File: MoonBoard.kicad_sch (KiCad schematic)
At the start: 52 parts, among them J1 TRRS, SW1 SW_SPST, SW2 SW_DIP_x04, U1 AMS1117-3.3, U2 74LS08, U3 STM32F303CBTx, Y1 16MHz

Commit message: tvs & less fun
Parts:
- removed J1: TRRS, Connector_Audio:Jack_3.5mm_PJ320E_Horizontal, symbol Connector_Audio:AudioJack4
- removed NT1: NetTie_2, NetTie:NetTie-2_SMD_Pad0.5mm, symbol Device:NetTie_2
- removed R1, R2, R3, R6, R7: 22, Resistor_SMD:R_0603_1608Metric, symbol Device:R_Small
- added U5 (x3): H5VU25U, MoonBoard:DFN2510, symbol Unified-Daughterboard-rescue:TPD4E05U06DQAR-acheronSymbols
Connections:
- net BOOT0: now also JP2.2 (B)
- net ENCODER_A: now also U5.1 (IO1), U5.10 (NC)
- net ENCODER_B: now also U5.2 (IO2), U5.9 (NC)
- net ENCODER_SW: now also ENCODER1.S2, U3.4 (PC15), U5.5 (D2-), U5.6 (NC); no longer ENCODER1.S1, U3.18 (PB0)
- net GND: now also ENCODER1.S1, U5.3 (GND), U5.3 (GND), U5.3 (GND), U5.8 (GND), U5.8 (GND), U5.8 (GND); no longer ENCODER1.S2
- net I2C1_SCL: now also U5.4 (D2+), U5.7 (NC)
- net I2C1_SDA: now also U5.5 (D2-), U5.6 (NC)
- net SWCLK: now also SWD1.4 (Pin_4), U5.1 (IO1), U5.10 (NC)
- net SWDIO: now also SWD1.6 (Pin_6), U5.1 (IO1), U5.10 (NC)
- net SWO: now also SWD1.2 (Pin_2), U5.2 (IO2), U5.9 (NC)
- net TIM8_CH1: no longer U2.12, U2.13
- net USB_D+: now also U5.4 (D2+), U5.7 (NC)
- net USB_D-: now also U5.5 (D2-), U5.6 (NC)
- net ~{RESET}: now also JP1.2 (B)
- net TIM8_CH2: now reaches U3.45 (PB8)
- net TIM8_CH2: now also U2.12, U2.13
- net USART1_CK: no longer names the net of U3.29 (PA8)
- net USART1_RX: no longer names the net of U3.31 (PA10)
- net USART1_TX: no longer names the net of U3.30 (PA9)
- new net: U5.2 (IO2), U5.9 (NC)
- new net: U5.4 (D2+), U5.7 (NC)
- no-connect marks 16 -> 17
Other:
- note removed: "Serial USART TRRS"
- moved on the sheet: NT2, R9, U2D

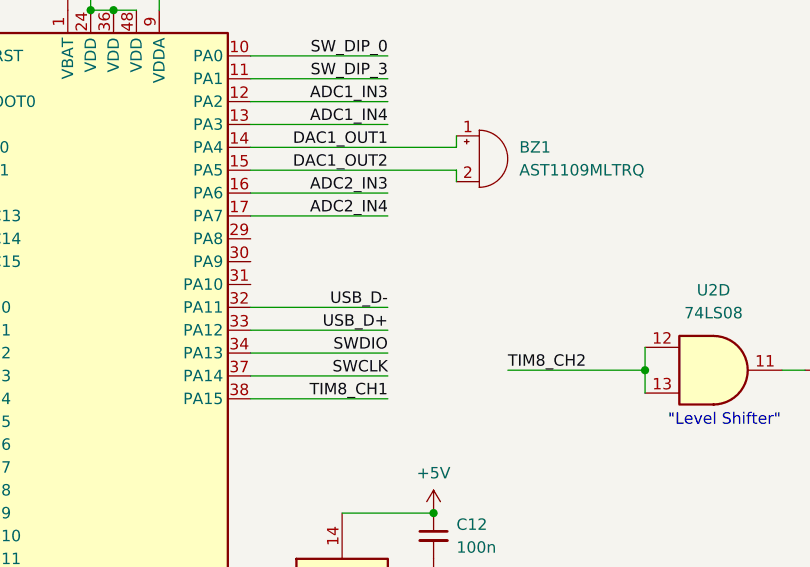
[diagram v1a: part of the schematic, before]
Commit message: add usb D+ pullup
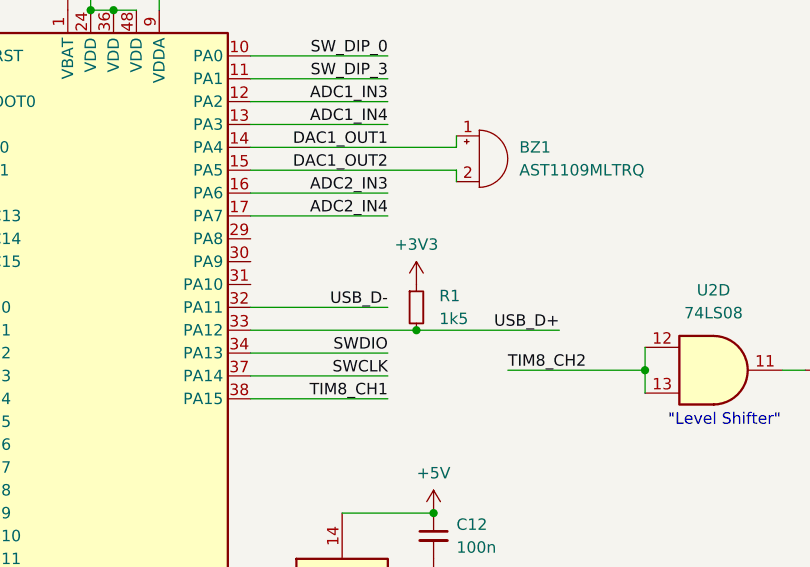
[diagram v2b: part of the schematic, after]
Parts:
- added R1: 1k5, Resistor_SMD:R_0402_1005Metric, symbol Device:R_Small
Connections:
- net +3V3: now also R1.1
- net USB_D+: now also R1.2
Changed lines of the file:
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@@
   (junction (at 160.02 149.86) (diameter 0) (color 0 0 0 0)
+  )
+  (junction (at 134.62 145.415) (diameter 0) (color 0 0 0 0)
   )
   (junction (at 336.55 113.03) (diameter 0) (color 0 0 0 0)
@@
     (stroke (width 0) (type default))
   )
-  (wire (pts (xy 116.205 145.415) (xy 131.445 145.415))
-    (stroke (width 0) (type default))
-  )
   (wire (pts (xy 139.065 128.905) (xy 139.065 127.635))
     (stroke (width 0) (type default))
@@
     (stroke (width 0) (type default))
   )
+  (wire (pts (xy 134.62 145.415) (xy 150.495 145.415))
+    (stroke (width 0) (type default))
+  )
   (wire (pts (xy 335.915 198.12) (xy 335.915 200.66))
     (stroke (width 0) (type default))
@@
   )
   (wire (pts (xy 53.34 27.94) (xy 56.134 27.94))
+    (stroke (width 0) (type default))
+  )
+  (wire (pts (xy 134.62 145.415) (xy 116.205 145.415))
     (stroke (width 0) (type default))
   )
@@
     (effects (font (size 1.27 1.27)) (justify right bottom))
   )
-  (label "USB_D+" (at 131.445 145.415 180) (fields_autoplaced)
+  (label "USB_D+" (at 150.495 145.415 180) (fields_autoplaced)
     (effects (font (size 1.27 1.27)) (justify right bottom))
   )
@@
     )
   )
+  (symbol (lib_id "Device:R_Small") (at 134.62 142.875 0) (unit 1)
+    (in_bom yes) (on_board yes) (dnp no) (fields_autoplaced)
+    (property "Reference" "R1" (at 137.16 141.605 0)
+      (effects (font (size 1.27 1.27)) (justify left))
+    )
+    (property "Value" "1k5" (at 137.16 144.145 0)
+      (effects (font (size 1.27 1.27)) (justify left))
+    )
+    (property "Footprint" "Resistor_SMD:R_0402_1005Metric" (at 134.62 142.875 0)
+      (effects (font (size 1.27 1.27)) hide)
+    )
+    (property "Datasheet" "~" (at 134.62 142.875 0)
+      (effects (font (size 1.27 1.27)) hide)
+    )
+    (pin "1")
+    (pin "2")
+    (instances
+      (project "MoonBoard"
+        (path "/bb706f4b-6d11-4e29-ae30-1a1ffddaf9f4"
+          (reference "R1") (unit 1)
+        )
+      )
+    )
+  )
   (symbol (lib_id "power:GND") (at 136.525 170.815 0) (unit 1)
     (in_bom yes) (on_board yes) (dnp no) (fields_autoplaced)
@@
         )
       )
+    )
+  )
+  (symbol (lib_id "power:+3V3") (at 134.62 140.335 0) (unit 1)
+    (in_bom yes) (on_board yes) (dnp no)
+    (property "Reference" "#PWR032" (at 134.62 144.145 0)
+      (effects (font (size 1.27 1.27)) hide)
+    )
+    (property "Value" "+3V3" (at 134.62 135.89 0)
+      (effects (font (size 1.27 1.27)))
+    )
+    (property "Footprint" "" (at 134.62 140.335 0)
+      (effects (font (size 1.27 1.27)) hide)
+    )
+    (property "Datasheet" "" (at 134.62 140.335 0)
+      (effects (font (size 1.27 1.27)) hide)
+    )
+    (pin "1")
+    (instances
+      (project "MoonBoard"
+        (path "/bb706f4b-6d11-4e29-ae30-1a1ffddaf9f4"
+          (reference "#PWR032") (unit 1)
+        )
+      )

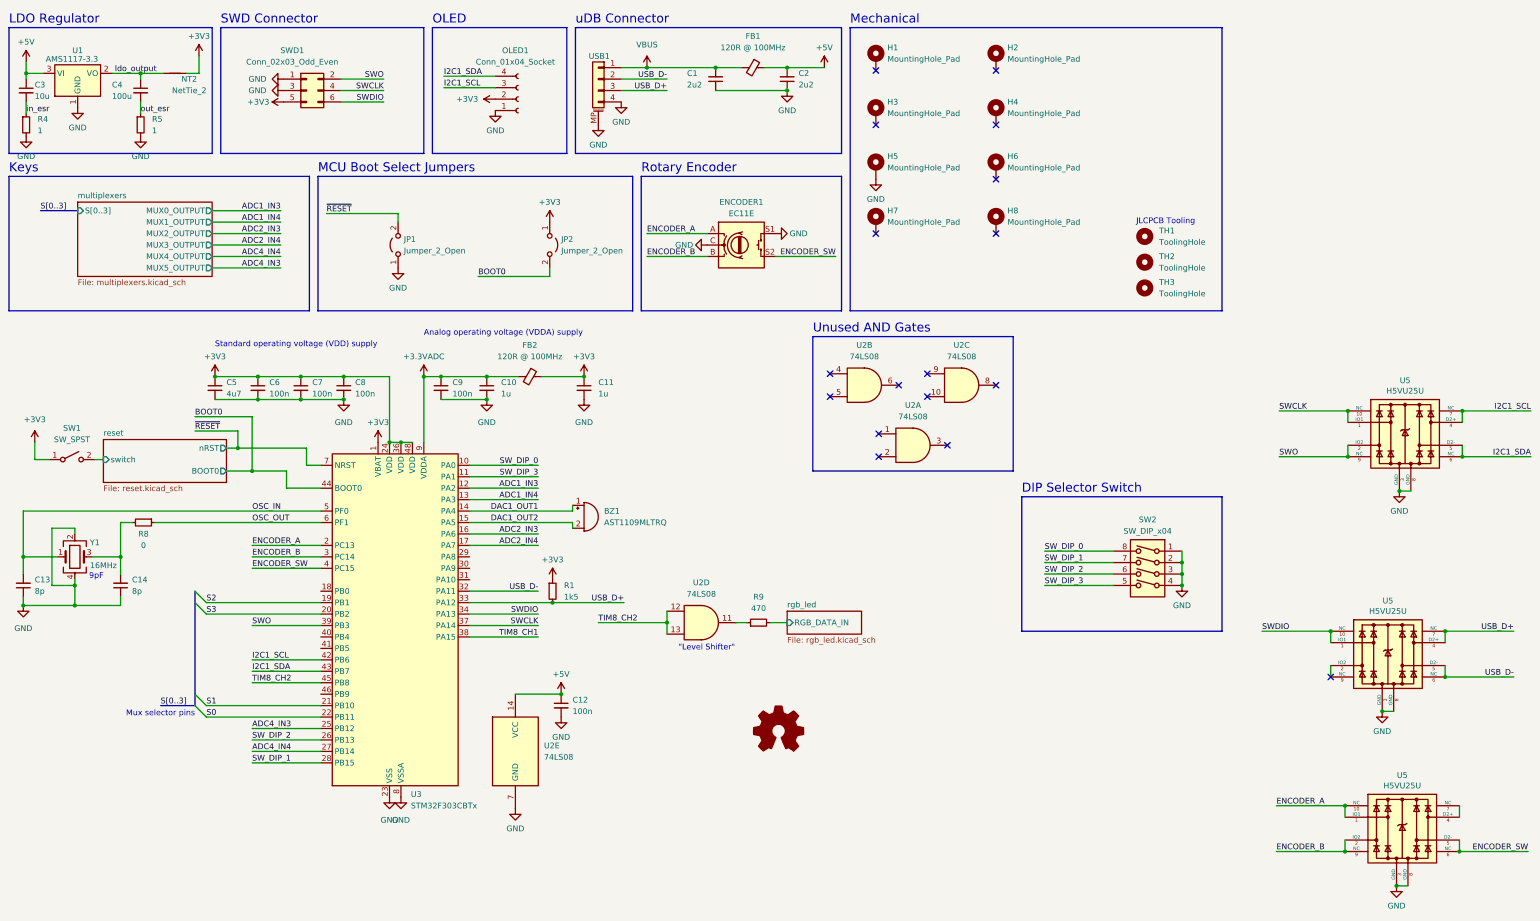
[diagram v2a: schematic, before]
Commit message: timer encoder mode
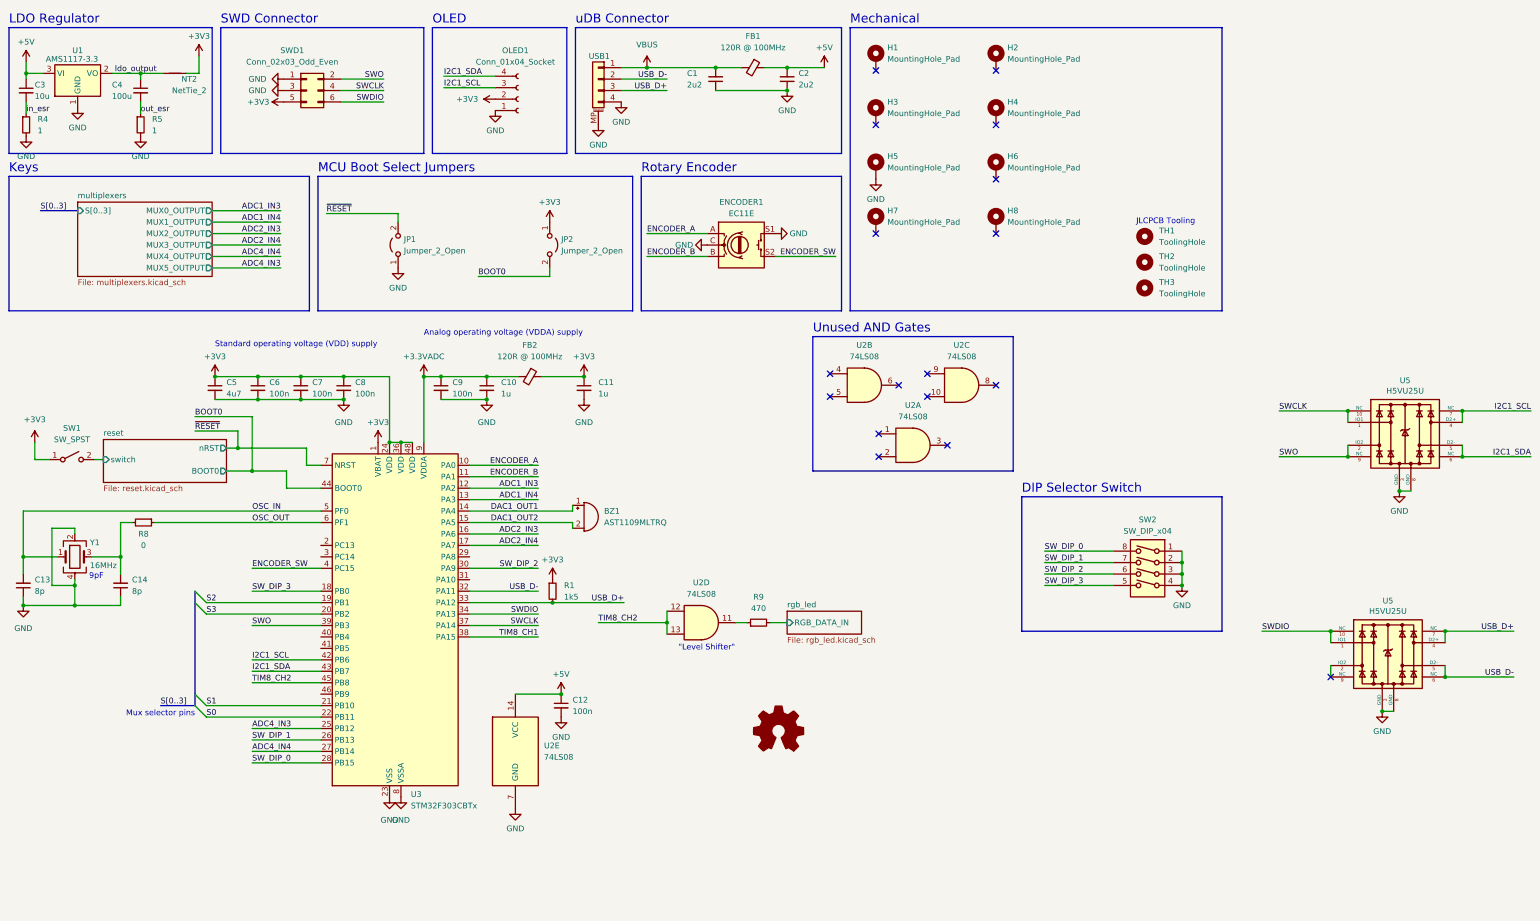
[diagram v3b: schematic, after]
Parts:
- removed U5: H5VU25U, MoonBoard:DFN2510, symbol Unified-Daughterboard-rescue:TPD4E05U06DQAR-acheronSymbols
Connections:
- net ENCODER_A: now also U3.10 (PA0); no longer U3.2 (PC13)
- net ENCODER_B: now also U3.11 (PA1); no longer U3.3 (PC14)
- net SW_DIP_0: now also U3.28 (PB15); no longer U3.10 (PA0)
- net SW_DIP_1: now also U3.26 (PB13); no longer U3.28 (PB15)
- net SW_DIP_2: now also U3.30 (PA9); no longer U3.26 (PB13)
- net SW_DIP_3: now also U3.18 (PB0); no longer U3.11 (PA1)
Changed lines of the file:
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@@
   (junction (at 120.015 100.33) (diameter 0) (color 0 0 0 0)
   )
-  (junction (at 310.515 200.66) (diameter 0) (color 0 0 0 0)
-  )
   (junction (at 136.525 165.735) (diameter 0) (color 0 0 0 0)
   )
-  (junction (at 335.915 200.66) (diameter 0) (color 0 0 0 0)
-  )
   (junction (at 69.215 95.25) (diameter 0) (color 0 0 0 0)
   )
@@
   (junction (at 186.69 26.67) (diameter 0) (color 0 0 0 0)
   )
-  (junction (at 321.945 208.28) (diameter 0) (color 0 0 0 0)
-  )
   (junction (at 98.425 109.855) (diameter 0) (color 0 0 0 0)
   )
@@
   (junction (at 170.815 26.67) (diameter 0) (color 0 0 0 0)
   )
-  (junction (at 310.515 190.5) (diameter 0) (color 0 0 0 0)
-  )
   (junction (at 274.32 139.065) (diameter 0) (color 0 0 0 0)
   )
@@
     (stroke (width 0) (type default))
   )
-  (wire (pts (xy 67.945 132.715) (xy 83.185 132.715))
+  (wire (pts (xy 131.445 114.935) (xy 116.205 114.935))
     (stroke (width 0) (type default))
   )
@@
     (stroke (width 0) (type default))
   )
-  (wire (pts (xy 67.945 135.255) (xy 83.185 135.255))
+  (wire (pts (xy 131.445 117.475) (xy 116.205 117.475))
     (stroke (width 0) (type default))
   )
@@
     (stroke (width 0) (type default))
   )
-  (wire (pts (xy 351.155 200.66) (xy 335.915 200.66))
-    (stroke (width 0) (type default))
-  )
   (wire (pts (xy 116.205 120.015) (xy 131.445 120.015))
     (stroke (width 0) (type default))
   )
-  (wire (pts (xy 310.515 190.5) (xy 310.515 193.04))
-    (stroke (width 0) (type default))
-  )
   (wire (pts (xy 97.155 34.29) (xy 87.63 34.29))
     (stroke (width 0) (type default))
   )
-  (wire (pts (xy 310.515 198.12) (xy 310.515 200.66))
-    (stroke (width 0) (type default))
-  )
   (wire (pts (xy 67.945 116.205) (xy 75.565 116.205))
     (stroke (width 0) (type default))
@@
     (stroke (width 0) (type default))
   )
-  (wire (pts (xy 131.445 114.935) (xy 116.205 114.935))
+  (wire (pts (xy 67.945 180.975) (xy 83.185 180.975))
     (stroke (width 0) (type default))
   )
@@
     (stroke (width 0) (type default))
   )
-  (wire (pts (xy 131.445 117.475) (xy 116.205 117.475))
+  (wire (pts (xy 67.945 142.875) (xy 83.185 142.875))
     (stroke (width 0) (type default))
   )
@@
     (stroke (width 0) (type default))
   )
-  (wire (pts (xy 295.275 200.66) (xy 310.515 200.66))
-    (stroke (width 0) (type default))
-  )
   (wire (pts (xy 67.945 116.205) (xy 67.945 104.14))
     (stroke (width 0) (type default))
@@
     (stroke (width 0) (type default))
   )
-  (wire (pts (xy 295.275 190.5) (xy 310.515 190.5))
-    (stroke (width 0) (type default))
-  )
-  (wire (pts (xy 321.945 208.28) (xy 324.485 208.28))
-    (stroke (width 0) (type default))
-  )
   (wire (pts (xy 336.55 102.87) (xy 351.79 102.87))
     (stroke (width 0) (type default))
@@
     (stroke (width 0) (type default))
   )
-  (wire (pts (xy 335.915 198.12) (xy 335.915 200.66))
-    (stroke (width 0) (type default))
-  )
   (wire (pts (xy 78.74 100.33) (xy 88.265 100.33))
     (stroke (width 0) (type default))
@@
     (stroke (width 0) (type default))
   )
-  (wire (pts (xy 67.945 180.975) (xy 83.185 180.975))
+  (wire (pts (xy 67.945 175.895) (xy 83.185 175.895))
     (stroke (width 0) (type default))
   )
@@
     (stroke (width 0) (type default))
   )
-  (wire (pts (xy 67.945 175.895) (xy 83.185 175.895))
+  (wire (pts (xy 131.445 137.795) (xy 116.205 137.795))
     (stroke (width 0) (type default))
   )
@@
     (stroke (width 0) (type default))
   )
-  (wire (pts (xy 335.915 190.5) (xy 335.915 193.04))
-    (stroke (width 0) (type default))
-  )
   (wire (pts (xy 116.205 122.555) (xy 131.445 122.555))
     (stroke (width 0) (type default))
@@
     (effects (font (size 1.27 1.27)) (justify left bottom))
   )
-  (label "ENCODER_B" (at 295.275 200.66 0) (fields_autoplaced)
-    (effects (font (size 1.27 1.27)) (justify left bottom))
-  )
   (label "out_esr" (at 43.18 36.83 0) (fields_autoplaced)
     (effects (font (size 1.27 1.27)) (justify left bottom))
   )
-  (label "SW_DIP_2" (at 67.945 175.895 0) (fields_autoplaced)
-    (effects (font (size 1.27 1.27)) (justify left bottom))
+  (label "SW_DIP_2" (at 131.445 137.795 180) (fields_autoplaced)
+    (effects (font (size 1.27 1.27)) (justify right bottom))
   )
   (label "ADC1_IN3" (at 131.445 120.015 180) (fields_autoplaced)
@@
     (effects (font (size 1.27 1.27)) (justify left bottom))
   )
-  (label "ENCODER_A" (at 67.945 132.715 0) (fields_autoplaced)
-    (effects (font (size 1.27 1.27)) (justify left bottom))
+  (label "ENCODER_A" (at 131.445 114.935 180) (fields_autoplaced)
+    (effects (font (size 1.27 1.27)) (justify right bottom))
   )
   (label "BOOT0" (at 55.245 104.14 0) (fields_autoplaced)
@@
     (effects (font (size 1.27 1.27)) (justify right bottom))
   )
-  (label "ENCODER_SW" (at 351.155 200.66 180) (fields_autoplaced)
-    (effects (font (size 1.27 1.27)) (justify right bottom))
-  )
   (label "USB_D-" (at 131.445 142.875 180) (fields_autoplaced)
     (effects (font (size 1.27 1.27)) (justify right bottom))
@@
     (effects (font (size 1.27 1.27)) (justify left bottom))
   )
-  (label "SW_DIP_1" (at 67.945 180.975 0) (fields_autoplaced)
+  (label "SW_DIP_1" (at 67.945 175.895 0) (fields_autoplaced)
     (effects (font (size 1.27 1.27)) (justify left bottom))
   )
@@
     (effects (font (size 1.27 1.27)) (justify right bottom))
   )
-  (label "ENCODER_A" (at 295.275 190.5 0) (fields_autoplaced)
-    (effects (font (size 1.27 1.27)) (justify left bottom))
-  )
   (label "ADC2_IN4" (at 74.295 66.04 180) (fields_autoplaced)
     (effects (font (size 1.27 1.27)) (justify right bottom))
@@
     (effects (font (size 1.27 1.27)) (justify right bottom))
   )
-  (label "SW_DIP_0" (at 131.445 114.935 180) (fields_autoplaced)
-    (effects (font (size 1.27 1.27)) (justify right bottom))
+  (label "SW_DIP_0" (at 67.945 180.975 0) (fields_autoplaced)
+    (effects (font (size 1.27 1.27)) (justify left bottom))
   )
   (label "ENCODER_A" (at 155.575 63.5 0) (fields_autoplaced)
@@
     (effects (font (size 1.27 1.27)) (justify right bottom))
   )
-  (label "ENCODER_B" (at 67.945 135.255 0) (fields_autoplaced)
-    (effects (font (size 1.27 1.27)) (justify left bottom))
+  (label "ENCODER_B" (at 131.445 117.475 180) (fields_autoplaced)
+    (effects (font (size 1.27 1.27)) (justify right bottom))
   )
   (label "S3" (at 57.785 147.955 0) (fields_autoplaced)
     (effects (font (size 1.27 1.27)) (justify left bottom))
   )
-  (label "SW_DIP_3" (at 131.445 117.475 180) (fields_autoplaced)
-    (effects (font (size 1.27 1.27)) (justify right bottom))
+  (label "SW_DIP_3" (at 67.945 142.875 0) (fields_autoplaced)
+    (effects (font (size 1.27 1.27)) (justify left bottom))
   )
   (label "SWO" (at 295.91 113.03 0) (fields_autoplaced)
@@
     )
   )
-  (symbol (lib_id "Unified-Daughterboard-rescue:TPD4E05U06DQAR-acheronSymbols") (at 323.215 195.58 0) (unit 1)
-    (in_bom yes) (on_board yes) (dnp no)
-    (property "Reference" "U5" (at 323.215 183.7436 0)
-      (effects (font (size 1.27 1.27)))
-    )
-    (property "Value" "H5VU25U" (at 323.215 186.055 0)
-      (effects (font (size 1.27 1.27)))
-    )
-    (property "Footprint" "MoonBoard:DFN2510" (at 323.215 168.91 0)
-      (effects (font (size 1.27 1.27)) hide)
-    )
-    (property "Datasheet" "" (at 323.215 195.58 0)
-      (effects (font (size 1.27 1.27)) hide)
-    )
-    (property "Manufacturer" "Texas Instruments" (at 323.215 171.45 0)
-      (effects (font (size 1.27 1.27)) hide)
-    )
-    (property "Manufacturer Part Number" "TPD4E05U06DQAR" (at 323.215 179.07 0)
-      (effects (font (size 1.27 1.27)) hide)
-    )
-    (property "Package" "uSON-10" (at 323.215 173.99 0)
-      (effects (font (size 1.27 1.27)) hide)
-    )
-    (property "LCSC Part Number" "C138714" (at 323.215 195.58 0)
-      (effects (font (size 1.27 1.27)) hide)
-    )
-    (pin "1")
-    (pin "10")
-    (pin "2")
-    (pin "3")
-    (pin "4")
-    (pin "5")
-    (pin "6")
-    (pin "7")
-    (pin "8")
-    (pin "9")
-    (instances
-      (project "MoonHub"
-        (path "/89c6bdf4-b90e-462a-98b5-5c238b339b0e"
-          (reference "U5") (unit 1)
-        )
-      )
-      (project "MoonBoard"
-        (path "/bb706f4b-6d11-4e29-ae30-1a1ffddaf9f4"
-          (reference "U12") (unit 1)
-        )
-      )
-      (project "UDB"
-        (path "/c4c12ac1-bf97-4e49-b99b-b461a52b064e"
-          (reference "U1") (unit 1)
-        )
-      )
-    )
-  )
   (symbol (lib_id "power:GND") (at 74.93 29.21 270) (unit 1)
     (in_bom yes) (on_board yes) (dnp no) (fields_autoplaced)
@@
         )
       )
-    )
-  )
-  (symbol (lib_id "power:GND") (at 321.945 208.28 0) (unit 1)
-    (in_bom yes) (on_board yes) (dnp no)
-    (property "Reference" "#PWR033" (at 321.945 214.63 0)
-      (effects (font (size 1.27 1.27)) hide)
-    )
-    (property "Value" "GND" (at 321.945 212.725 0)
-      (effects (font (size 1.27 1.27)))
-    )
-    (property "Footprint" "" (at 321.945 208.28 0)
-      (effects (font (size 1.27 1.27)) hide)
-    )
-    (property "Datasheet" "" (at 321.945 208.28 0)
-      (effects (font (size 1.27 1.27)) hide)
-    )
-    (pin "1")
-    (instances
-      (project "MoonHub"
-        (path "/89c6bdf4-b90e-462a-98b5-5c238b339b0e"
-          (reference "#PWR033") (unit 1)
-        )
-      )
-      (project "MoonBoard"
-        (path "/bb706f4b-6d11-4e29-ae30-1a1ffddaf9f4"
-          (reference "#PWR029") (unit 1)
-        )
-      )
